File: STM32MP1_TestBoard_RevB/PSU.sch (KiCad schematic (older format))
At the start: 30 parts, among them J11 USB_C_Receptacle_USB2.0, J9 Barrel_Jack, U3 SE8233X2, U4 TPS54202DDC, U5 SiP3250x, U6 SiP3250x

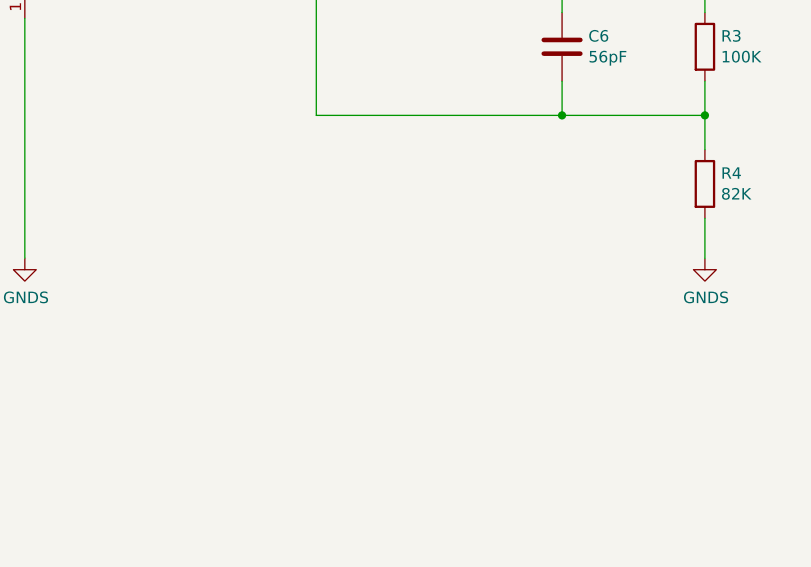
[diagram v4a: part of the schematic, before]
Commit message: Tested RevB power supply
Original BuckReg TPS54202
Replacement BuckReg TPS563200
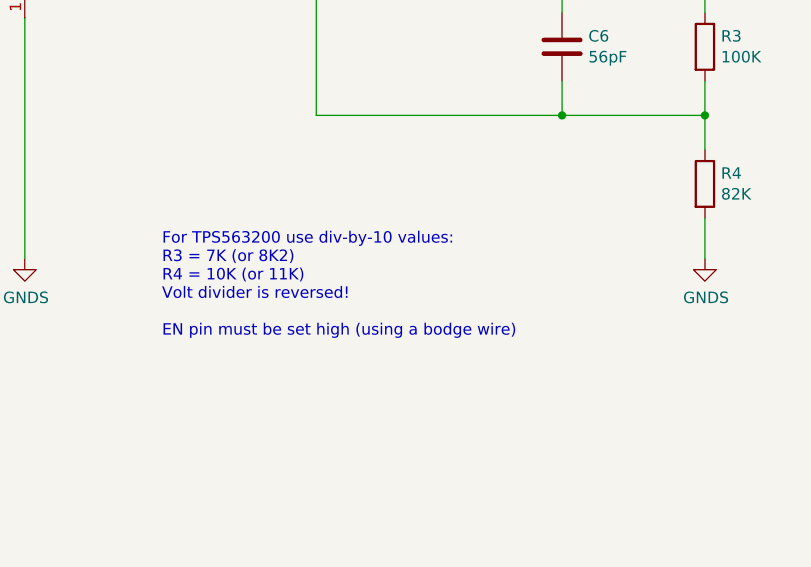
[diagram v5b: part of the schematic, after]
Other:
- note added: "For TPS563200 use div-by-10 values:\nR3 = 7K (or 8K2)\nR4 = 10K (or 11K)\nVolt divider is reversed!\n\nEN pin must be set high (using a bodge wire)"
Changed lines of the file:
@@
 	1    0    0    -1
 $EndComp
+Text Notes 9250 6100 0    50   ~ 0
+For TPS563200 use div-by-10 values:\nR3 = 7K (or 8K2)\nR4 = 10K (or 11K)\nVolt divider is reversed!\n\nEN pin must be set high (using a bodge wire)
 $EndSCHEMATC

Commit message: fixed BOM error
R4 listed with capacitor part number, corrected to resistor part number
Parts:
- R4: LCSC C1542 -> C25571
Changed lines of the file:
@@
 F 4 "~" H 11625 5425 50  0001 C CNN "Mfr"
 F 5 "~" H 11625 5425 50  0001 C CNN "PartNo"
-F 6 "C1542" H 11625 5425 50  0001 C CNN "LCSC"
+F 6 "C25571" H 11625 5425 50  0001 C CNN "LCSC"
 F 7 "~" H 11625 5425 50  0001 C CNN "Comment"
 F 8 "~" H 11625 5425 50  0001 C CNN "Mouser"
@@
 	13000 4400 12250 4400
 Connection ~ 12250 4400
-Wire Wire Line
-	8650 4700 8650 5750
 $Comp
 L power:GNDS #PWR05
@@
 	6525 5250 6525 5750
 Connection ~ 6975 4300
-Wire Wire Line
-	6975 4300 8250 4300
 $Comp
 L Connector:Barrel_Jack J9
@@
 	1    0    0    -1
 $EndComp
-NoConn ~ 8250 4500
 Wire Wire Line
 	13450 4400 15225 4400
@@
 Text Notes 9250 6100 0    50   ~ 0
 For TPS563200 use div-by-10 values:\nR3 = 7K (or 8K2)\nR4 = 10K (or 11K)\nVolt divider is reversed!\n\nEN pin must be set high (using a bodge wire)
+Wire Wire Line
+	6975 4300 8250 4300
+Wire Wire Line
+	8650 4700 8650 5750
+NoConn ~ 8250 4500
 $EndSCHEMATC
